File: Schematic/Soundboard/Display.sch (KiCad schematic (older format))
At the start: 1 part, among them U1 STM32f429IIT6-units

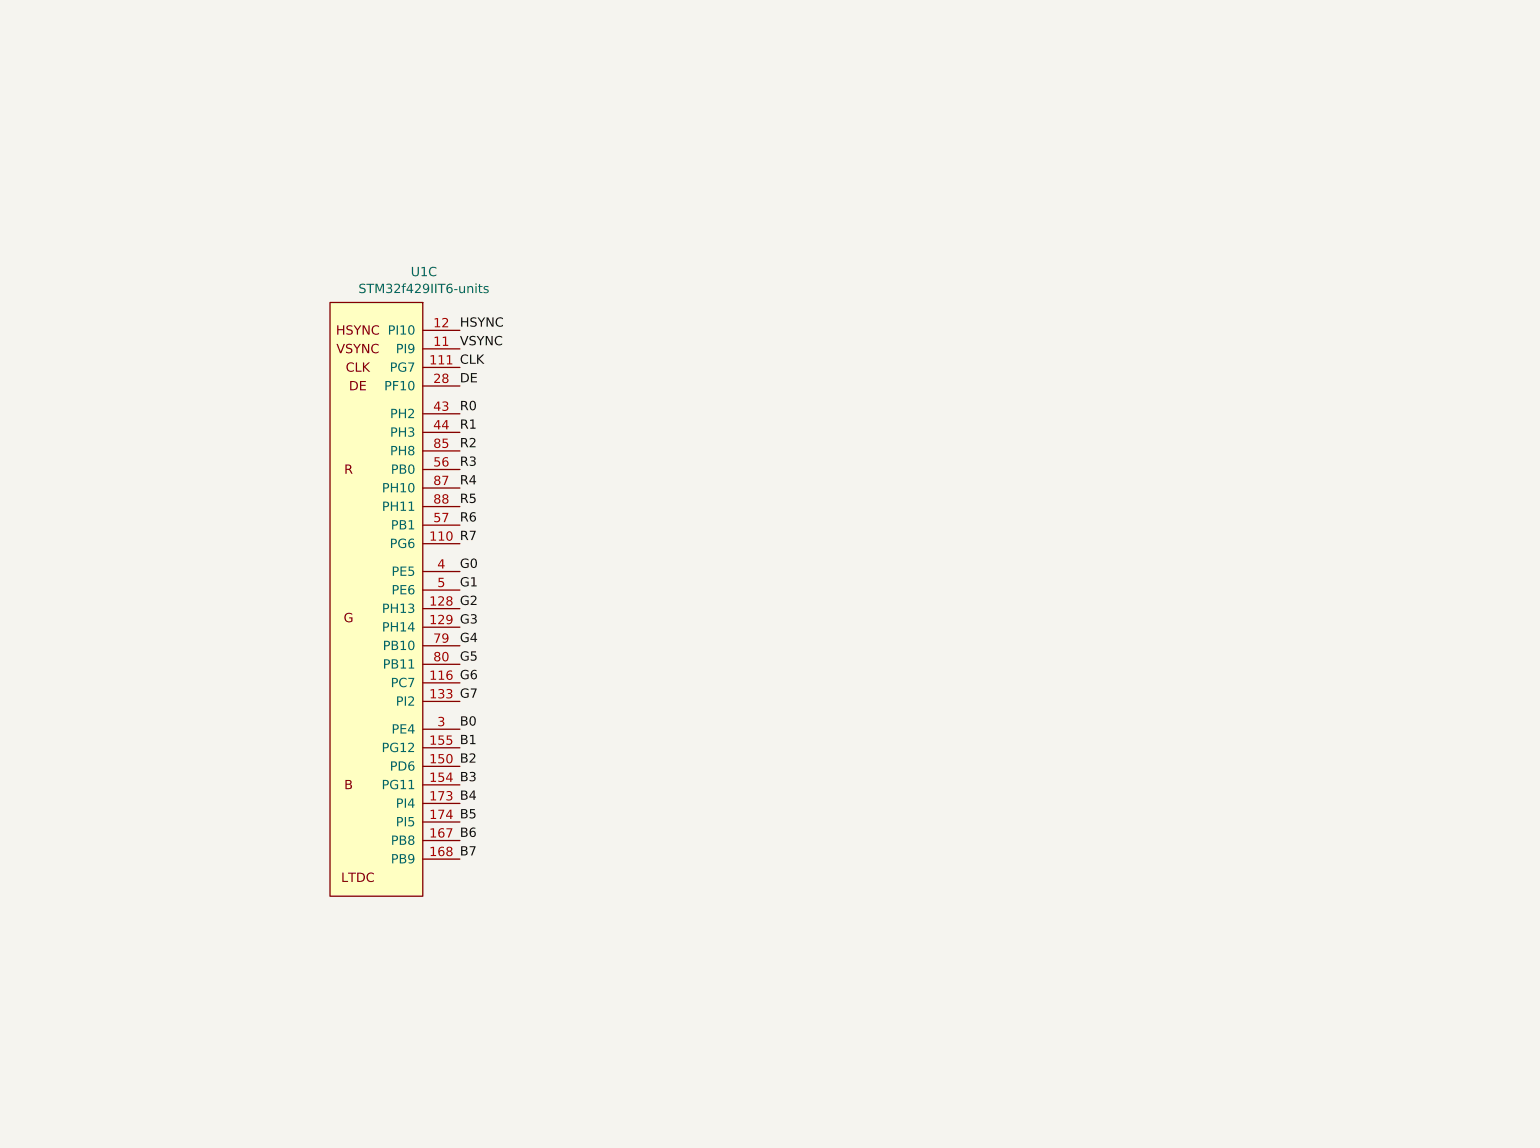
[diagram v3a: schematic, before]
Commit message: Choose display. Complete schematic
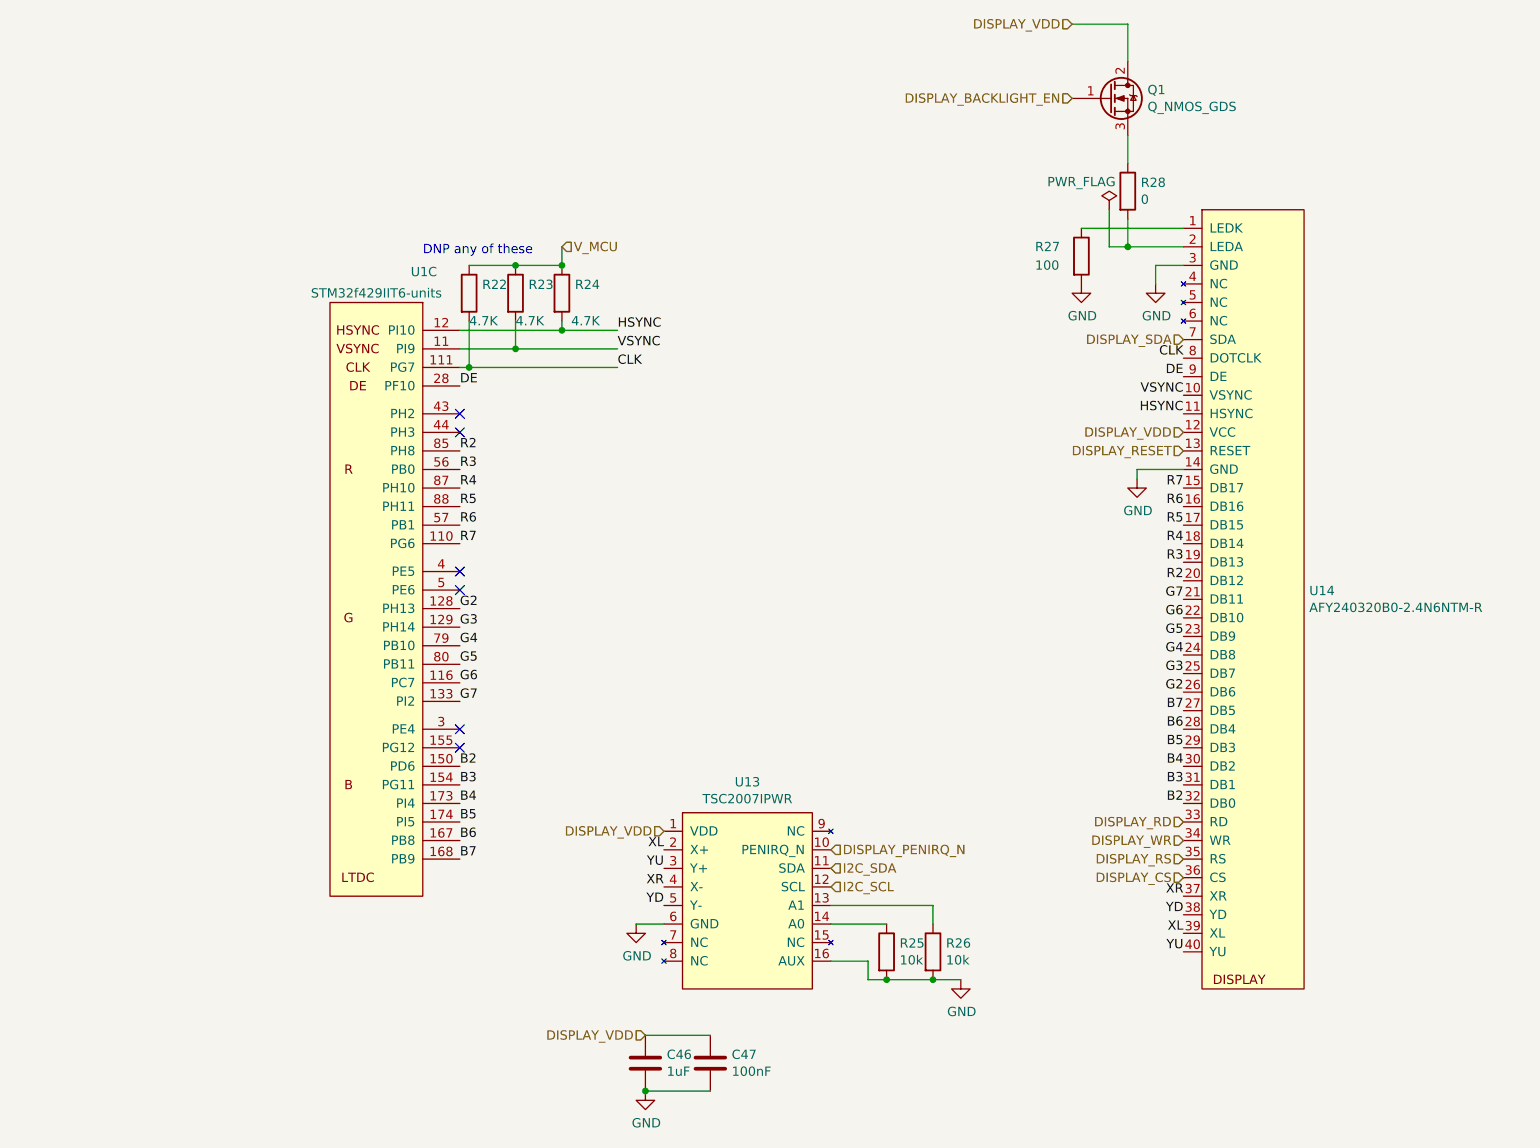
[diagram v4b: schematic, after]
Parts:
- added C46: 1uF, Capacitor_SMD:C_0603_1608Metric_Pad1.05x0.95mm_HandSolder, symbol Device:C
- added C47: 100nF, Capacitor_SMD:C_0603_1608Metric_Pad1.05x0.95mm_HandSolder, symbol Device:C
- added Q1: Q_NMOS_GDS, Package_TO_SOT_SMD:SOT-23, symbol Device:Q_NMOS_GDS
- added R22, R23, R24: 4.7K, Resistor_SMD:R_0603_1608Metric_Pad1.05x0.95mm_HandSolder, symbol Device:R
- added R25, R26: 10k, Resistor_SMD:R_0603_1608Metric_Pad1.05x0.95mm_HandSolder, symbol Device:R
- added R27: 100, Resistor_SMD:R_0603_1608Metric_Pad1.05x0.95mm_HandSolder, symbol Device:R
- added R28: 0, Resistor_SMD:R_0603_1608Metric_Pad1.05x0.95mm_HandSolder, symbol Device:R
- added U13: TSC2007IPWR, Package_SO:TSSOP-16_4.4x5mm_P0.65mm, symbol Soundboard:TSC2007IPWR
- added U14: AFY240320B0-2.4N6NTM-R, Connector_FFC-FPC:Hirose_FH12-40S-0.5SH_1x40-1MP_P0.50mm_Horizontal, symbol Soundboard:AFY240320B0-2.4N6NTM-R
- U1: footprint (none) -> Package_QFP:LQFP-176_24x24mm_P0.5mm
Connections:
- net B2: now also U14.32 (DB0)
- net B3: now also U14.31 (DB1)
- net B4: now also U14.30 (DB2)
- net B5: now also U14.29 (DB3)
- net B6: now also U14.28 (DB4)
- net B7: now also U14.27 (DB5)
- net CLK: now also R22.2, U14.8 (DOTCLK)
- net DE: now also U14.9 (DE)
- net G2: now also U14.26 (DB6)
- net G3: now also U14.25 (DB7)
- net G4: now also U14.24 (DB8)
- net G5: now also U14.23 (DB9)
- net G6: now also U14.22 (DB10)
- net G7: now also U14.21 (DB11)
- net HSYNC: now also R24.2, U14.11 (HSYNC)
- net R2: now also U14.20 (DB12)
- net R3: now also U14.19 (DB13)
- net R4: now also U14.18 (DB14)
- net R5: now also U14.17 (DB15)
- net R6: now also U14.16 (DB16)
- net R7: now also U14.15 (DB17)
- net VSYNC: now also R23.2, U14.10 (VSYNC)
- net B0: no longer names the net of U1.3 (PE4)
- net B1: no longer names the net of U1.155 (PG12)
- net G0: no longer names the net of U1.4 (PE5)
- net G1: no longer names the net of U1.5 (PE6)
- net R0: no longer names the net of U1.43 (PH2)
- net R1: no longer names the net of U1.44 (PH3)
- new net: R27.1, U14.1 (LEDK)
- new net: R28.2, U14.2 (LEDA)
- new net: Q1.3 (S), R28.1
- new net: R26.1, U13.13 (A1)
- new net: R25.1, U13.14 (A0)
- new net DISPLAY_BACKLIGHT_EN: Q1.1 (G)
- new net DISPLAY_CS: U14.36 (CS)
- new net DISPLAY_PENIRQ_N: U13.10 (PENIRQ_N)
- new net DISPLAY_RD: U14.33 (RD)
- new net DISPLAY_RESET: U14.13 (RESET)
- new net DISPLAY_RS: U14.35 (RS)
- new net DISPLAY_SDA: U14.7 (SDA)
- new net DISPLAY_VDD: C46.1, C47.1, Q1.2 (D), U13.1 (VDD), U14.12 (VCC)
- new net DISPLAY_WR: U14.34 (WR)
- new net GND: C46.2, C47.2, R25.2, R26.2, R27.2, U13.16 (AUX), U13.6 (GND), U14.14 (GND), U14.3 (GND)
- new net I2C_SCL: U13.12 (SCL)
- new net I2C_SDA: U13.11 (SDA)
- new net V_MCU: R22.1, R23.1, R24.1
- new net XL: U13.2 (X+), U14.39 (XL)
- new net XR: U13.4 (X-), U14.37 (XR)
- new net YD: U13.5 (Y-), U14.38 (YD)
- new net YU: U13.3 (Y+), U14.40 (YU)
- no-connect marks 0 -> 6
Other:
- note added: "DNP any of these\n"
